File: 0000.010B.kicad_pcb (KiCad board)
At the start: 2 copper layers, 80 x 70 mm, 85 parts, among them J1 PH254, J5 M3, J6 M3, J7 M3, J9 M3, Q1 50N10, Q2 50N10, U1 IRS2184, U2 TLIN4029A, U3 LMR71915, U4 INA280A1xDCK, U5 L78L05_SOT89, U8 ATtiny806-S

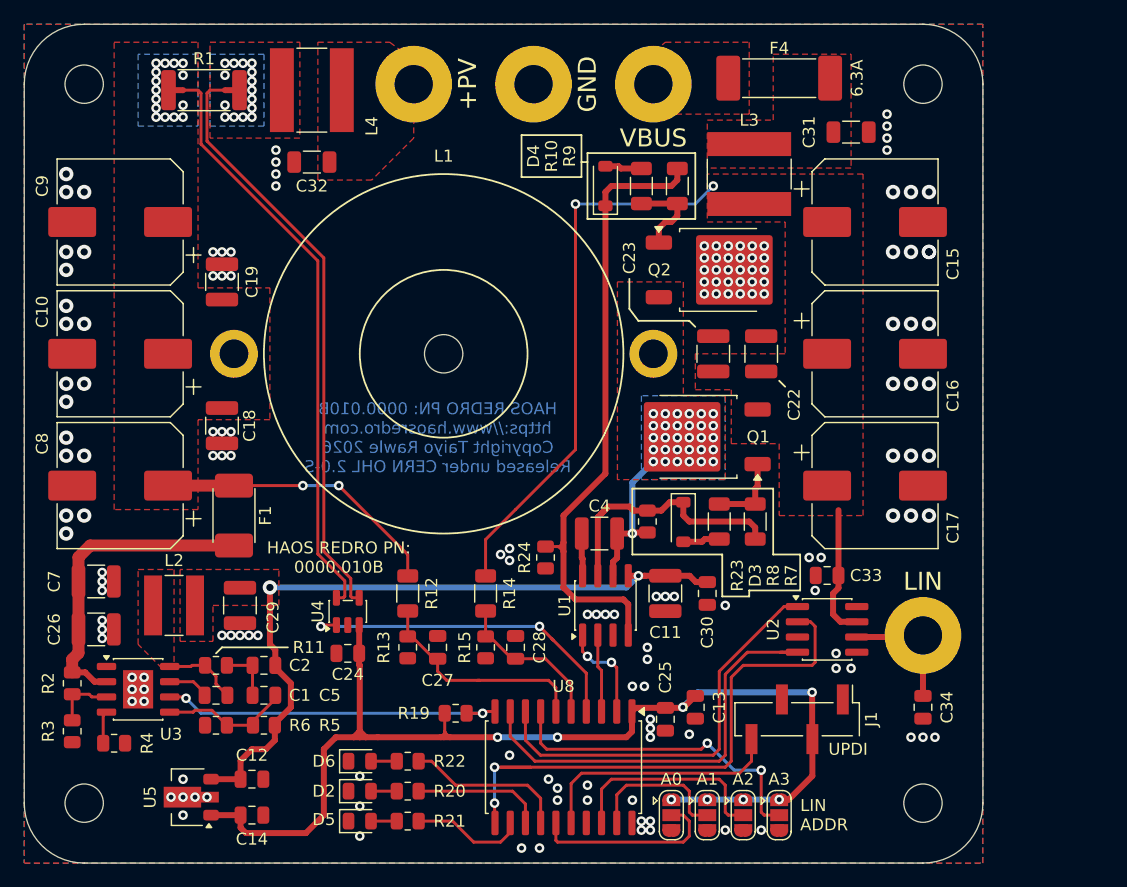
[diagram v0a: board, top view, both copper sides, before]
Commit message: Changed MCU to AT90PWM316-16M - much higher PWM frequency than the Atiny. Smaller inductor and replaced electrolytic capacitors with ceramic.
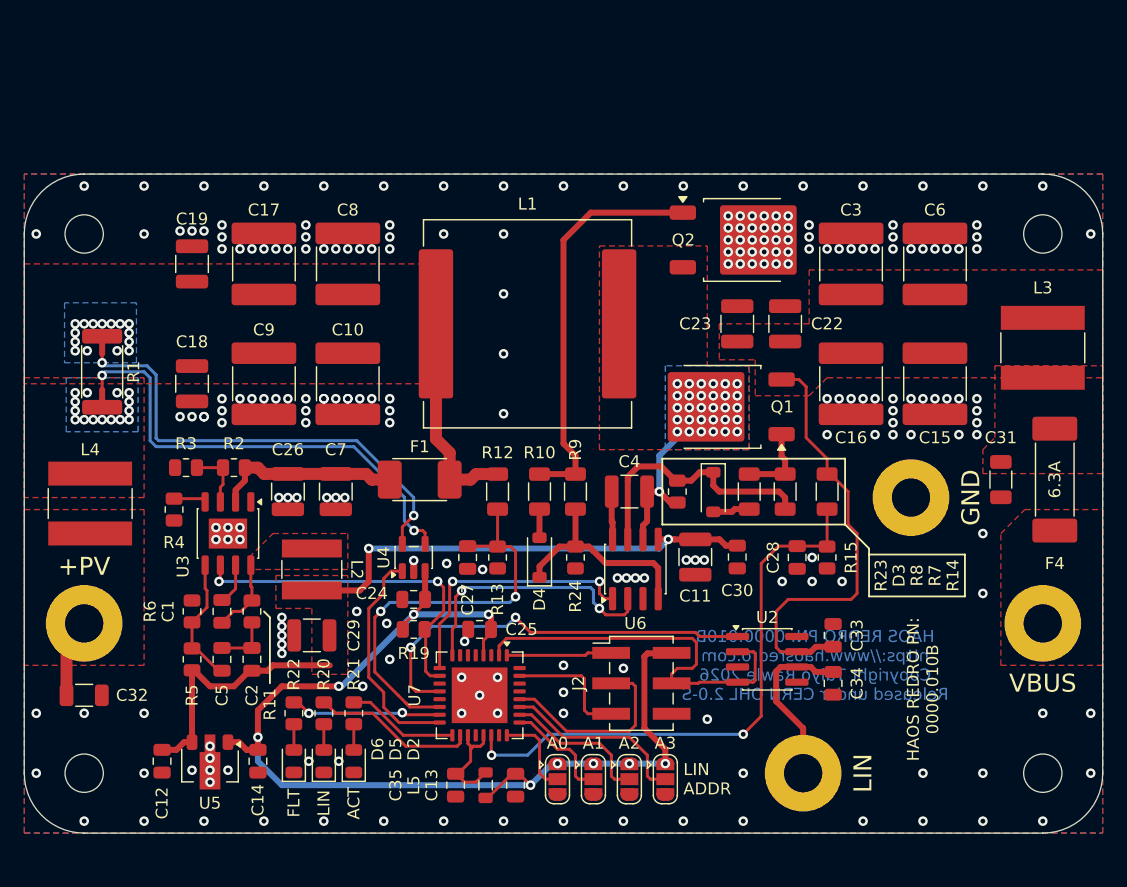
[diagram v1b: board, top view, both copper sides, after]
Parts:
- removed J1: PH254, Connector_PinHeader_2.54mm:PinHeader_1x04_P2.54mm_Vertical_SMD_Pin1Left
- removed U1: IRS2184, Package_SO:SOIC-8_3.9x4.9mm_P1.27mm
- removed U8: ATtiny806-S, Package_SO:SOIC-20W_7.5x12.8mm_P1.27mm
- added C3: 156, Capacitor_SMD:C_2220_5750Metric, F.Cu at (164.0, 77.5)
- added C35: 104, Capacitor_SMD:C_0805_2012Metric, F.Cu at (131.0, 121.0)
- added C6: 156, Capacitor_SMD:C_2220_5750Metric, F.Cu at (171.0, 77.5)
- added J2: AVR-ISP-6, Connector_PinHeader_2.54mm:PinHeader_2x03_P2.54mm_Vertical_SMD, F.Cu at (146.5, 112.5)
- added L5: 10, Inductor_SMD:L_0805_2012Metric, F.Cu at (133.5, 121.0)
- added U6: IRS2181, Package_SO:SOIC-8_3.9x4.9mm_P1.27mm, F.Cu at (146.0, 103.0)
- added U7: AT90PWM316-16M, Package_DFN_QFN:QFN-32-1EP_7x7mm_P0.65mm_EP4.65x4.65mm, F.Cu at (133.0, 113.5)
- C10, C15, C16, C17, C8, C9: value 100 -> 156; footprint Capacitor_SMD:CP_Elec_10x10 -> Capacitor_SMD:C_2220_5750Metric
- D5: value RED -> GRN
- L1: footprint HR_parts:L_TOROID_D30_2P_H_2 -> Inductor_SMD:L_Vishay_IHLP-6767
- moved J6 55.5 mm to (180.0, 107.5)
- moved C17 54.3 mm to (115.0, 77.5), turned to 90 degrees
- moved J5 52.7 mm to (100.0, 107.5)
- moved C32 48.4 mm to (100.0, 113.5), turned to 0 degrees
- moved J7 46.7 mm to (169.0, 97.0)
- moved F4 40.6 mm to (181.0, 95.5), turned to 90 degrees
- moved L4 39.1 mm to (100.5, 97.5), turned to -90 degrees
- moved C31 31.6 mm to (176.5, 95.5), turned to -90 degrees
- moved D4 31.5 mm to (138.0, 102.0)
- moved R14 29.7 mm to (162.0, 96.5)
- moved R15 29.5 mm to (162.0, 102.0)
- moved L3 28.5 mm to (180.0, 84.5), turned to -90 degrees
- moved NT2 27.7 mm to (101.5, 88.5), turned to 90 degrees
- moved R10 26.9 mm to (138.0, 96.5), turned to -90 degrees
- moved R9 26.9 mm to (141.0, 96.5), turned to -90 degrees
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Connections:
- C17 pad 1: VBUS -> +PV
- R20 pad 1: Net-(U8-PC1) -> /Controller/LED1
- R21 pad 1: Net-(U8-PC0) -> /Controller/LED0
- R22 pad 1: Net-(U8-PC2) -> /Controller/LED2
- U2 pad 2: Net-(U2-EN) -> Net-(J2-MOSI)
- U2 pad 4: Net-(U2-TXD) -> Net-(J2-MOSI)
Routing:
- net Net-(U2-EN): track 46.3 -> 0.00 mm, vias 2 -> 0
- net Net-(U2-TXD): track 36.1 -> 0.00 mm
- net Net-(D4-K): track 52.7 -> 17.9 mm
- net /Controller/VB_SENSE: track 13.2 -> 47.5 mm, vias 0 -> 2
- net Net-(J2-MOSI): track 0.00 -> 33.5 mm
- net Net-(Q2-G): track 7.19 -> 33.9 mm
- net /PWML: track 0.00 -> 22.4 mm, vias 0 -> 2
- net /PWMH: track 0.00 -> 22.2 mm, vias 0 -> 2
- net Net-(J1-Pin_4): track 21.0 -> 0.00 mm
- net VBUS: track 57.4 -> 36.9 mm, vias 2 -> 0
- net Net-(J2-SCK): track 0.00 -> 16.4 mm
- net /Controller/PV_SENSE: track 19.1 -> 35.1 mm, vias 0 -> 2
- net /Controller/LED1: track 0.00 -> 13.7 mm
- net Net-(U8-PC2): track 13.5 -> 0.00 mm
- net /Controller/LED2: track 0.00 -> 12.6 mm, vias 0 -> 2
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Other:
- board size 80 x 70 mm -> 90 x 55 mm

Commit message: Temperature sensor added as the AT90PWM316 does not have an internal one.
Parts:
- added C36: 104, Capacitor_SMD:C_0805_2012Metric, F.Cu at (158.0, 102.0)
- added U1: MCP9700Ax-ETT, Package_TO_SOT_SMD:SOT-23, F.Cu at (161.5, 102.0)
- moved R14 15.2 mm to (166.5, 111.0)
- moved C28 13.5 mm to (169.5, 111.0)
- moved R15 13.5 mm to (172.0, 111.0)
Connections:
- U7 pad 23: unconnected-(U7-PB3-Pad23) -> /Controller/A0
- U7 pad 24: /Controller/A0 -> /Controller/A1
- U7 pad 25: /Controller/A1 -> /Controller/A2
- U7 pad 26: /Controller/A2 -> /Controller/A3
- U7 pad 27: /Controller/A3 -> /Controller/TEMP
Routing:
- net /Controller/TEMP: track 0.00 -> 34.0 mm, vias 0 -> 2
- net +5V: track 92.9 -> 111.2 mm, vias 9 -> 11
- net VBUS: track 36.9 -> 33.9 mm
- net /Controller/VB_SENSE: track 47.5 -> 45.6 mm
- net Net-(J2-MOSI): track 33.5 -> 32.3 mm
- net /Controller/A1: track 9.18 -> 10.2 mm
- net Net-(J2-SCK): track 16.4 -> 15.8 mm
- net GND: vias 226 -> 233
